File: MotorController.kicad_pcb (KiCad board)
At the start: 2 copper layers, 95 x 102.5 mm, 133 parts, among them IC1 ft234xd, IC2 A3921KLPTR-T, IC3 A3921KLPTR-T, J1 SH, J10 PA, J11 XT30, J2 USB_B_Micro, J3 XA, J4 XA, J5 3020-10-0300-00, J6 SH, J7 SH, J8 3020-10-0300-00, J9 XA, Q1 GSFQ6806, Q2 GSFQ6806, Q3 GSFQ6806, Q4 SFS9Z34, Q5 GSFQ6806, Q6 SFS9Z34, SW2 BLACK, SW3 BLACK, SW4 2MS1-T1-B4-VS2-Q-E-S, SW5 RED, U1 LXES11D, U2 STM32F303K8Tx, U3 TJA1441AT, U4 TPSM13604HNDWR, U5 LMZ12002EXT, Y1 32M

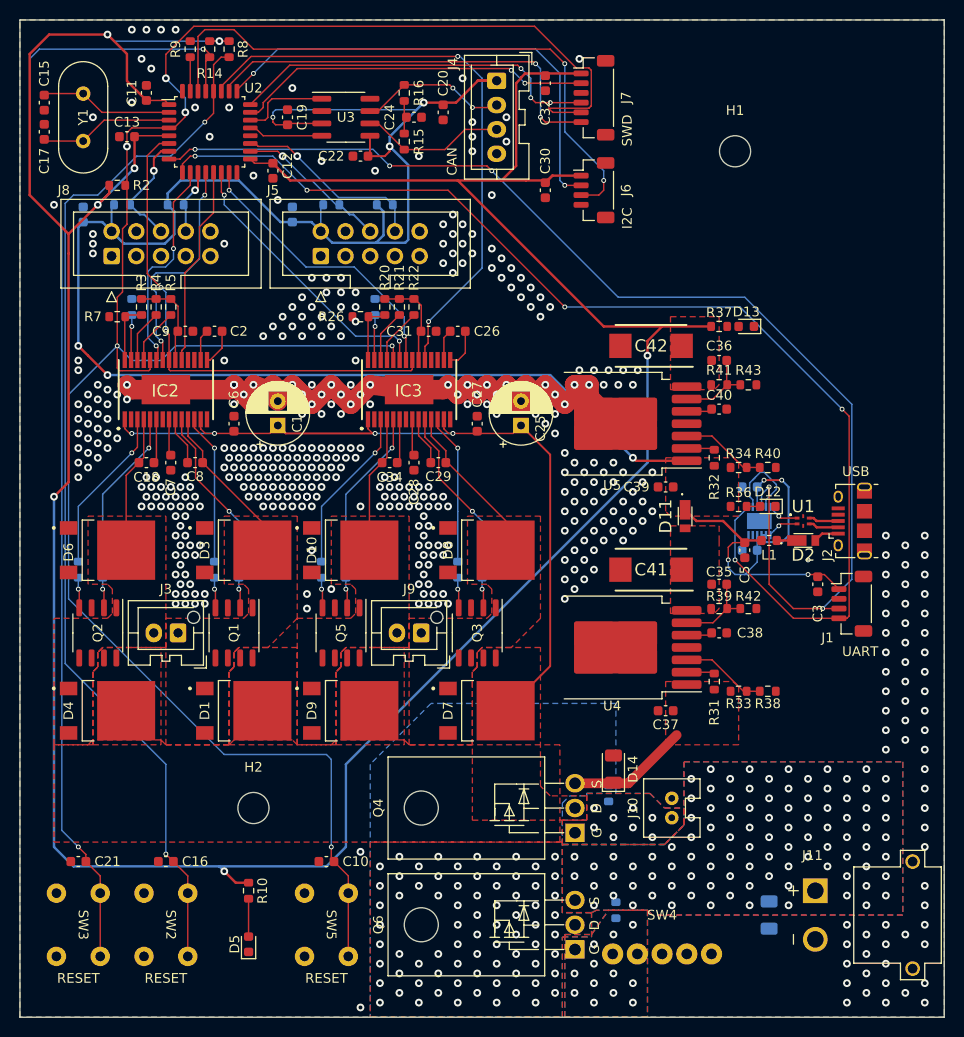
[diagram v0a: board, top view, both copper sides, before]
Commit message: DRC 通してシルク以外のエラーを修正
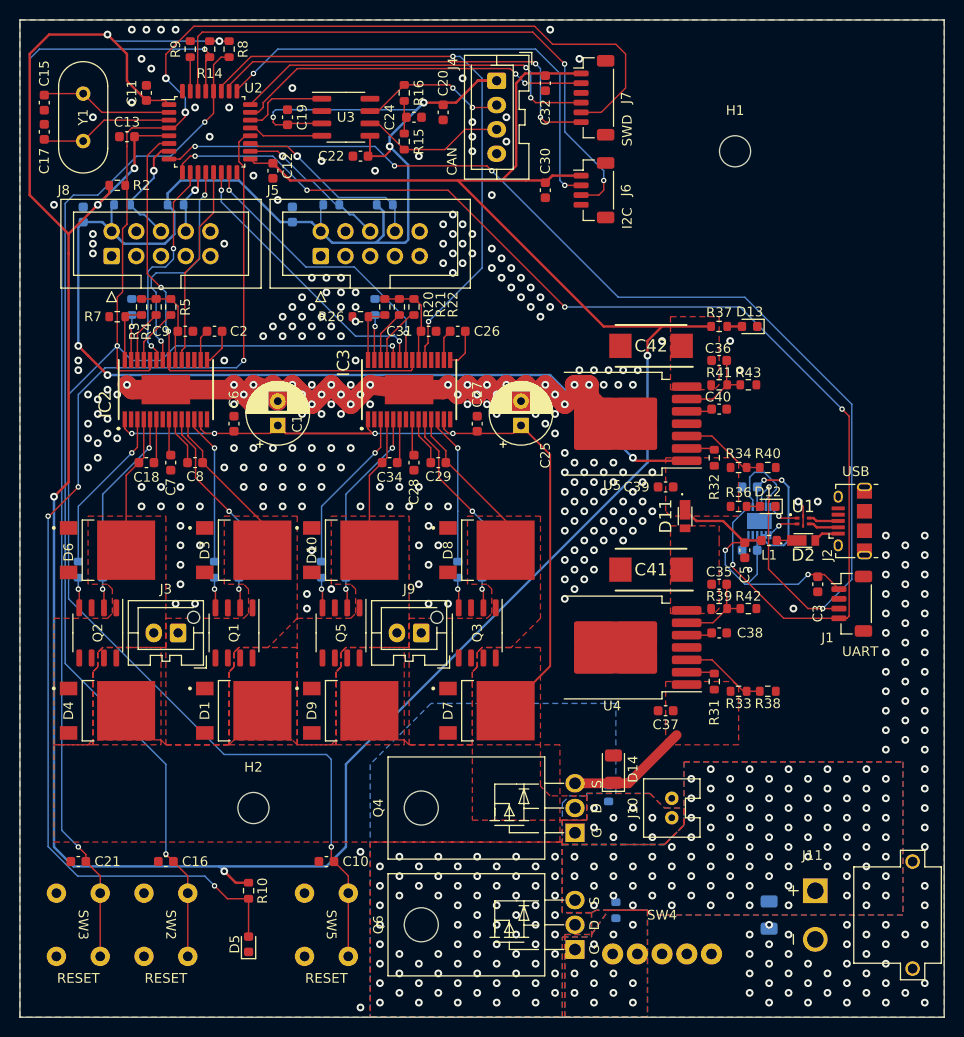
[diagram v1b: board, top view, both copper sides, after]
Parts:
- moved D13 0.35 mm to (90.0, 46.5)
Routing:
- net Net-(D5-A): track 3.89 -> 117.1 mm, vias 0 -> 4
- net GND: track 74.0 -> 76.7 mm, vias 451 -> 343
- net +5V: track 220.8 -> 222.7 mm
- net Net-(D13-A): track 0.00 -> 1.52 mm
- net Net-(IC1-TXD): track 121.7 -> 122.5 mm, vias 6 -> 5
- net Net-(IC1-RXD): track 124.3 -> 123.7 mm
- net Net-(IC1-3V3OUT): track 14.7 -> 15.3 mm
- net NRST: track 215.4 -> 215.7 mm, vias 6 -> 5
- net Net-(J7-Pin_4): track 39.0 -> 38.8 mm, vias 3 -> 2

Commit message: 画像と PDF の更新
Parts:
- moved H1 12.0 mm to (100.0, 25.0)
- moved H2 3.16 mm to (36.0, 95.0)
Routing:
- net GND: track 76.7 -> 78.9 mm, vias 343 -> 365
